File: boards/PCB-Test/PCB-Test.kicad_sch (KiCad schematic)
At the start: 5 parts, among them U1 74HC137, U2 74HC137, U3 74HC137, U4 ATmega32-16A, U5 ATmega32-16M

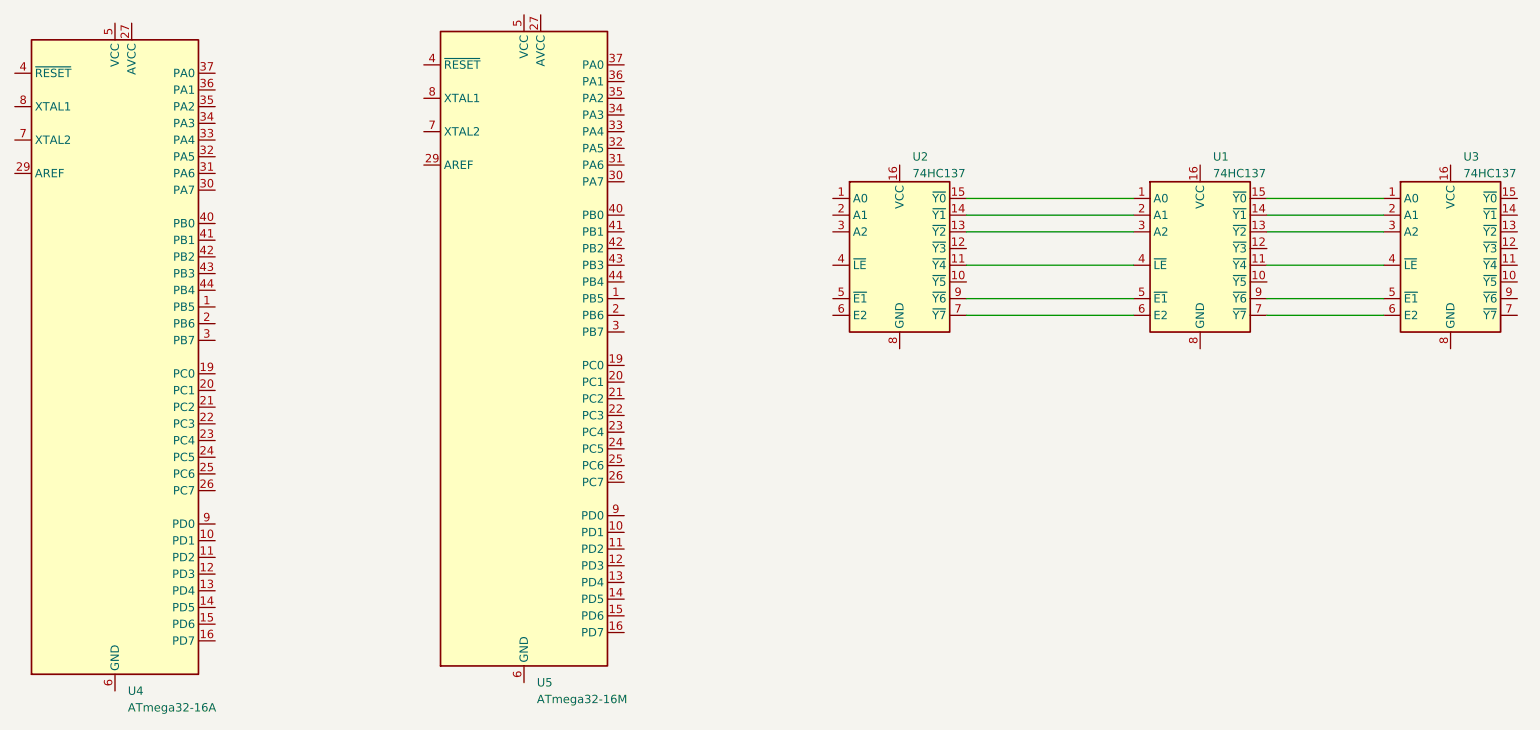
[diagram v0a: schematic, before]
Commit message: Update PCB test board with different track sizes
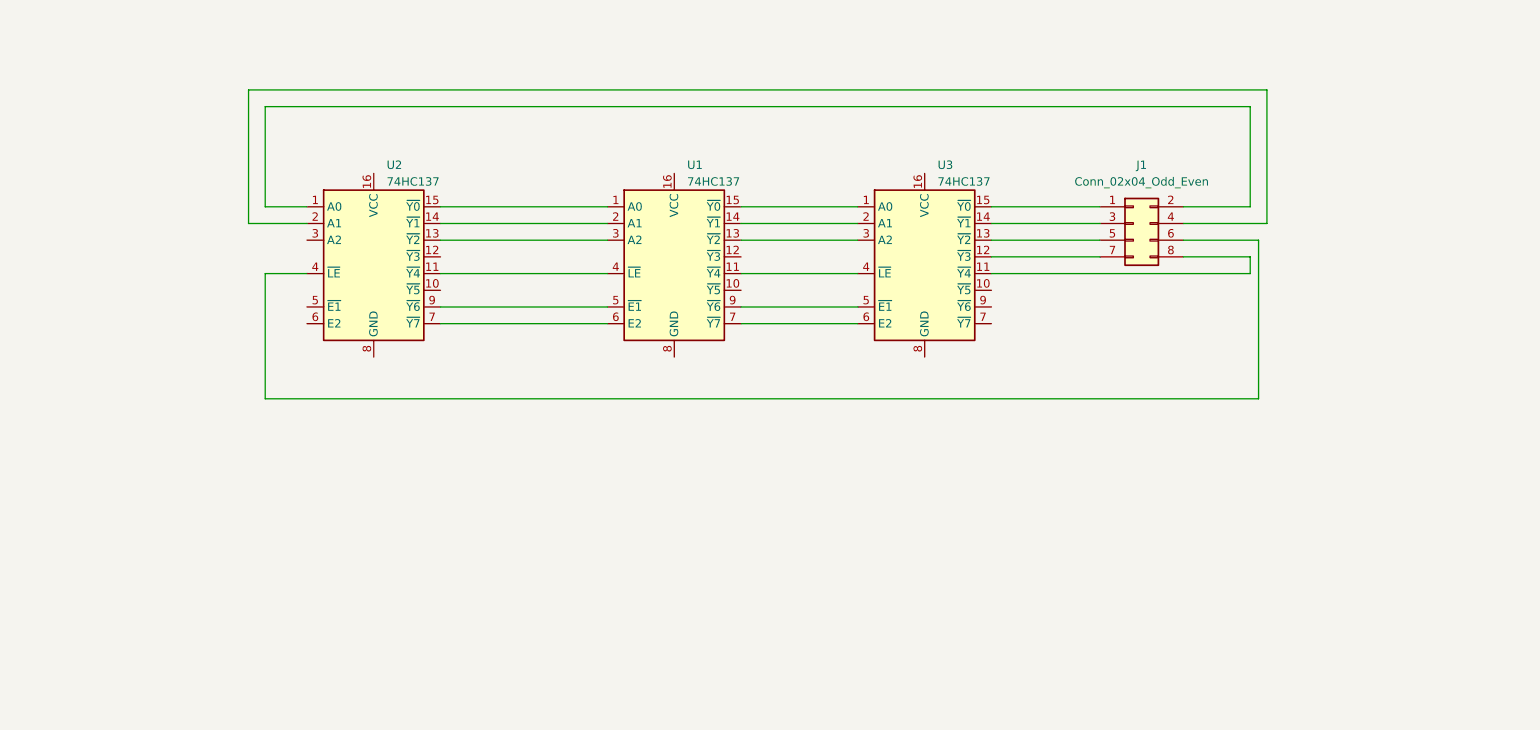
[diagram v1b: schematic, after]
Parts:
- removed U4: ATmega32-16A, Package_QFP:TQFP-44_10x10mm_P0.8mm, symbol MCU_Microchip_ATmega:ATmega32-16A
- removed U5: ATmega32-16M, Package_DFN_QFN:QFN-44-1EP_7x7mm_P0.5mm_EP5.2x5.2mm, symbol MCU_Microchip_ATmega:ATmega32-16M
- added J1: Conn_02x04_Odd_Even, Connector_IDC:IDC-Header_2x04_P2.54mm_Vertical, symbol Connector_Generic:Conn_02x04_Odd_Even
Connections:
- net at U3.11 (~{Y4}): now also J1.8 (Pin_8)
- net at U3.12 (~{Y3}): now also J1.7 (Pin_7)
- net at U3.13 (~{Y2}): now also J1.5 (Pin_5)
- net at U3.14 (~{Y1}): now also J1.3 (Pin_3)
- net at U3.15 (~{Y0}): now also J1.1 (Pin_1)
- net at U2.1 (A0): now also J1.2 (Pin_2)
- net at U2.2 (A1): now also J1.4 (Pin_4)
- net at U2.4 (~{LE}): now also J1.6 (Pin_6)
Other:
- moved on the sheet: U1, U2, U3

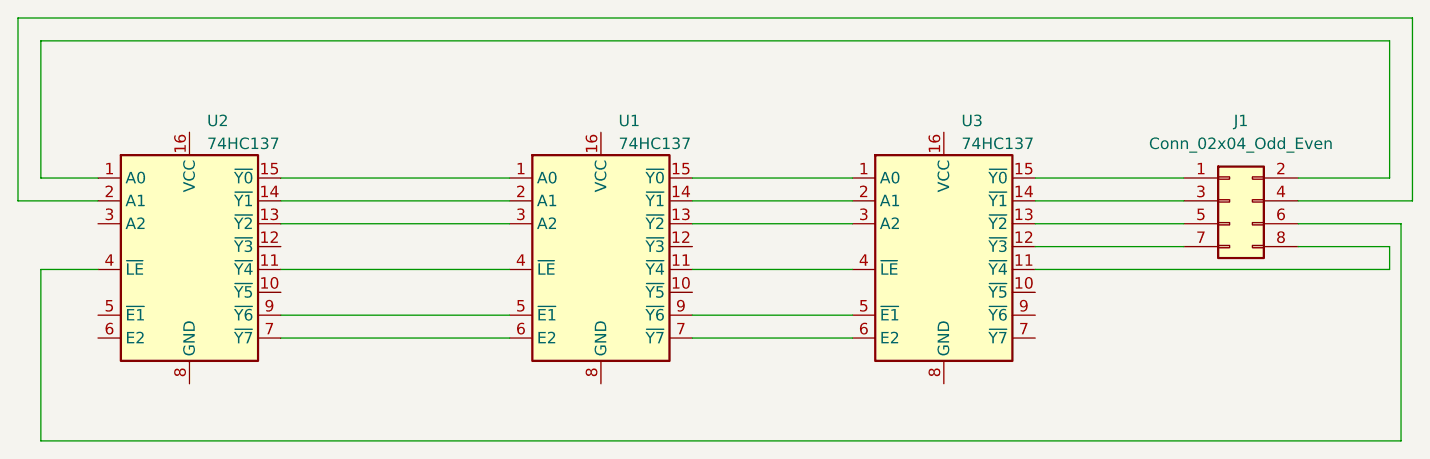
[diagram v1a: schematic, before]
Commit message: Updated test PCB for milling, remove too small footprint
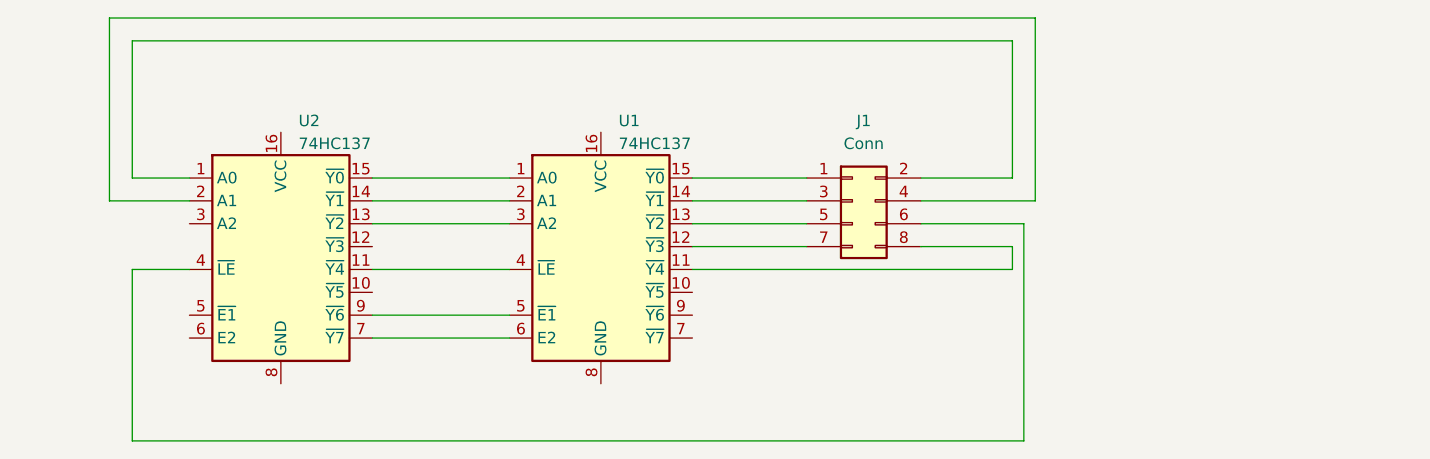
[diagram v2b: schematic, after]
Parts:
- removed U3: 74HC137, Package_SO:SSOP-16_5.3x6.2mm_P0.65mm, symbol 74xx:74HC137
- J1: value Conn_02x04_Odd_Even -> Conn; footprint Connector_IDC:IDC-Header_2x04_P2.54mm_Vertical -> Connector_PinSocket_2.54mm:PinSocket_2x04_P2.54mm_Vertical
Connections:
- net at U1.15 (~{Y0}): now also J1.1 (Pin_1)
- net at J1.8 (Pin_8): now also U1.11 (~{Y4})
- net at J1.7 (Pin_7): now also U1.12 (~{Y3})
- net at J1.5 (Pin_5): now also U1.13 (~{Y2})
- net at J1.3 (Pin_3): now also U1.14 (~{Y1})
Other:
- moved on the sheet: J1, U2

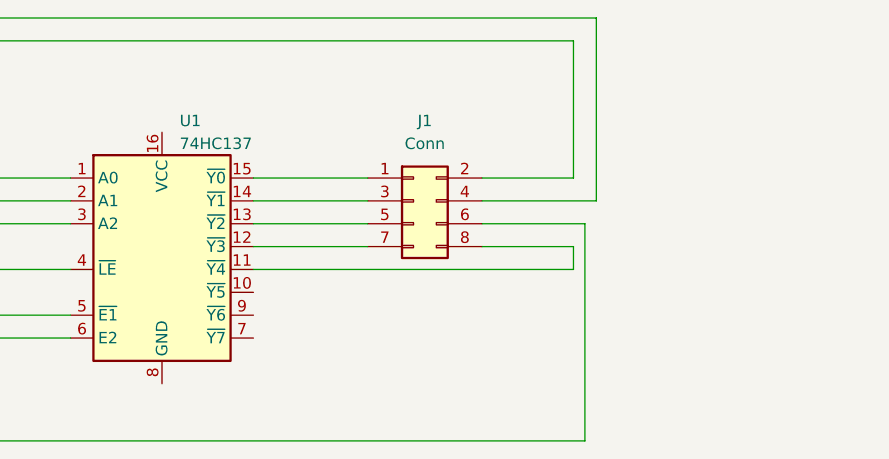
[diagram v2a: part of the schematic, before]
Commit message: Added new PCB design rule templates for PCB milling
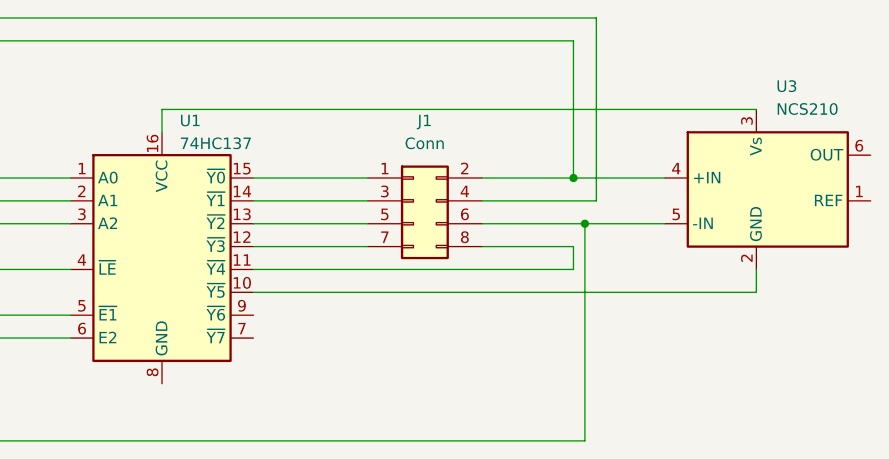
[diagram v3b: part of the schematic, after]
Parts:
- added U3: NCS210, Package_TO_SOT_SMD:SOT-363_SC-70-6_Handsoldering, symbol Amplifier_Current:NCS210
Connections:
- net at J1.2 (Pin_2), U2.1 (A0): now also U3.4 (+IN)
- net at J1.6 (Pin_6), U2.4 (~{LE}): now also U3.5 (-IN)
- net at U1.10 (~{Y5}): now also U3.2 (GND)
- net at U1.16 (VCC): now also U3.3 (Vs)
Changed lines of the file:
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@@
 	(generator_version "8.0")
 	(paper "A4")
+	(junction
+		(at 193.04 86.36)
+		(diameter 0)
+		(color 0 0 0 0)
+	)
+	(junction
+		(at 191.77 81.28)
+		(diameter 0)
+		(color 0 0 0 0)
+	)
 	(wire
 		(pts
@@
 	(wire
 		(pts
+			(xy 212.09 73.66) (xy 146.05 73.66)
+		)
+		(stroke
+			(width 0)
+			(type default)
+		)
+	)
+	(wire
+		(pts
 			(xy 191.77 66.04) (xy 93.98 66.04)
 		)
@@
 	(wire
 		(pts
+			(xy 191.77 81.28) (xy 201.93 81.28)
+		)
+		(stroke
+			(width 0)
+			(type default)
+		)
+	)
+	(wire
+		(pts
 			(xy 93.98 110.49) (xy 93.98 91.44)
 		)
@@
 	(wire
 		(pts
+			(xy 193.04 86.36) (xy 201.93 86.36)
+		)
+		(stroke
+			(width 0)
+			(type default)
+		)
+	)
+	(wire
+		(pts
 			(xy 120.65 91.44) (xy 135.89 91.44)
 		)
@@
 	(wire
 		(pts
+			(xy 146.05 73.66) (xy 146.05 76.2)
+		)
+		(stroke
+			(width 0)
+			(type default)
+		)
+	)
+	(wire
+		(pts
 			(xy 120.65 83.82) (xy 135.89 83.82)
 		)
@@
 	(wire
 		(pts
+			(xy 212.09 93.98) (xy 156.21 93.98)
+		)
+		(stroke
+			(width 0)
+			(type default)
+		)
+	)
+	(wire
+		(pts
+			(xy 212.09 91.44) (xy 212.09 93.98)
+		)
+		(stroke
+			(width 0)
+			(type default)
+		)
+	)
+	(wire
+		(pts
 			(xy 191.77 81.28) (xy 191.77 66.04)
 		)
@@
 		)
 	)
+	(symbol
+		(lib_id "Amplifier_Current:NCS210")
+		(at 212.09 83.82 0)
+		(unit 1)
+		(exclude_from_sim no)
+		(in_bom yes)
+		(on_board yes)
+		(dnp no)
+		(fields_autoplaced yes)
+		(property "Reference" "U3"
+			(at 214.2841 71.12 0)
+			(effects
+				(font
+					(size 1.27 1.27)
+				)
+				(justify left)
+			)
+		)
+		(property "Value" "NCS210"
+			(at 214.2841 73.66 0)
+			(effects
+				(font
+					(size 1.27 1.27)
+				)
+				(justify left)
+			)
+		)
+		(property "Footprint" "Package_TO_SOT_SMD:SOT-363_SC-70-6_Handsoldering"
+			(at 212.09 83.82 0)
+			(effects
+				(font
+					(size 1.27 1.27)
+				)
+				(hide yes)
+			)
+		)
+		(property "Datasheet" "https://www.onsemi.com/pub/Collateral/NCS210R-D.PDF"
+			(at 212.09 83.82 0)
+			(effects
+				(font
+					(size 1.27 1.27)
+				)
+				(hide yes)
+			)
+		)
+		(property "Description" "Current-Shunt Monitor, Voltage Output, Bi-Directional Zero-Drift, 200V/V Gain, SC-70-6"
+			(at 212.09 83.82 0)
+			(effects
+				(font
+					(size 1.27 1.27)
+				)
+				(hide yes)
+			)
+		)
+		(pin "3"
+		)
+		(pin "1"
+		)
+		(pin "4"
+		)
+		(pin "6"
+		)
+		(pin "2"
+		)
+		(pin "5"
+		)
+		(instances
+			(project "PCB-Test"
+				(path "/593abbd4-ef60-40c7-bfd9-9972546c7088"
+					(reference "U3")
+					(unit 1)
+				)
+			)
+		)
+	)
